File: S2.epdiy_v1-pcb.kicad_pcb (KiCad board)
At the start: 4 copper layers, 99.1 x 58.9 mm, 80 parts, among them J1 USB_C_Receptacle_USB2.0, J2 Jack-DC, SW1 RESET, SW2 BOOT, U1 MCP1700-1202E_SOT23, U11 TP4056, U2 ESP32-S2-WROVER, U3 TPS651851RSLR, U6 ED060XC5, U7 TPS2113APW

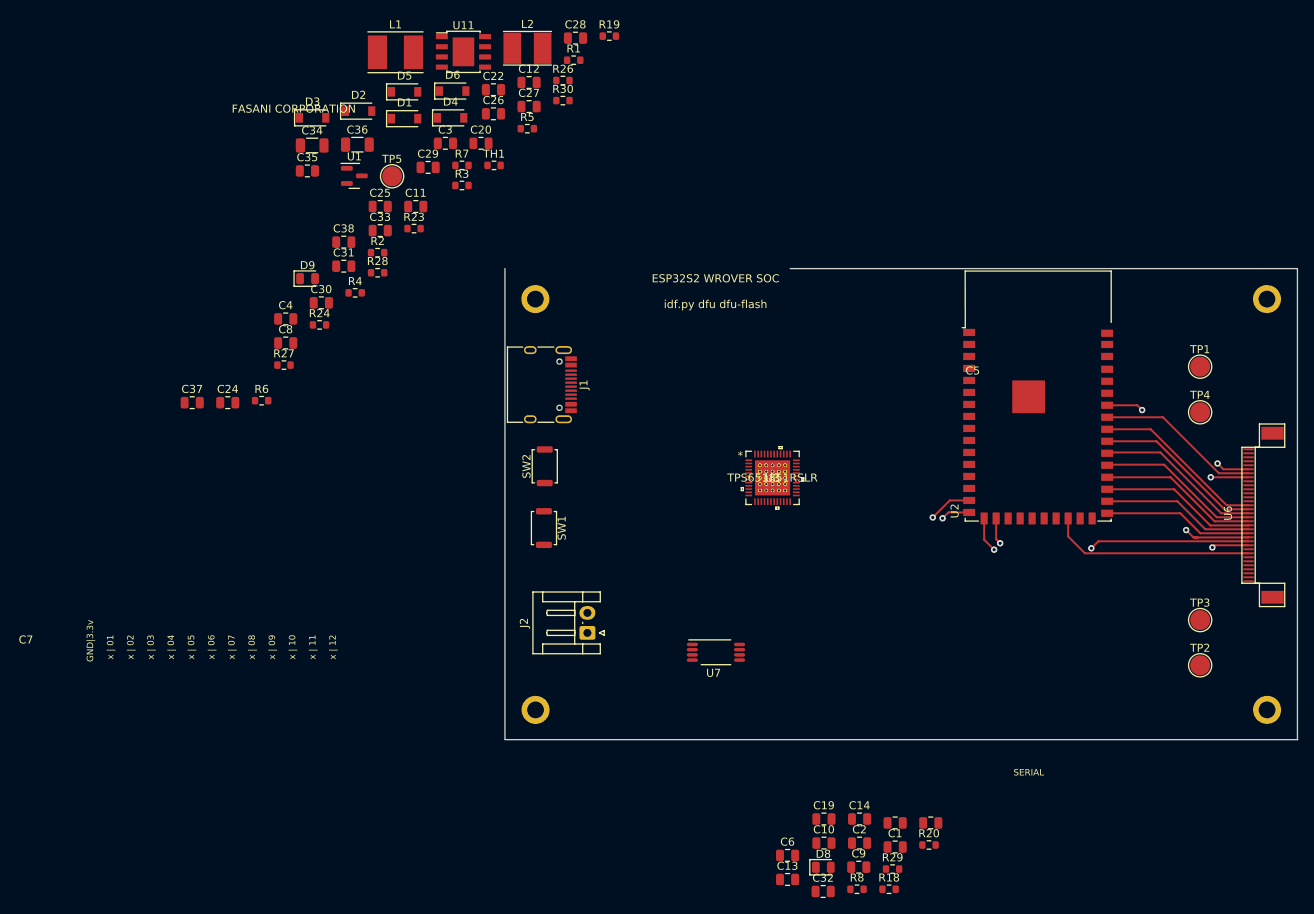
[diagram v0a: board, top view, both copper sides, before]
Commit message: Routing v1. Pending ERC pass
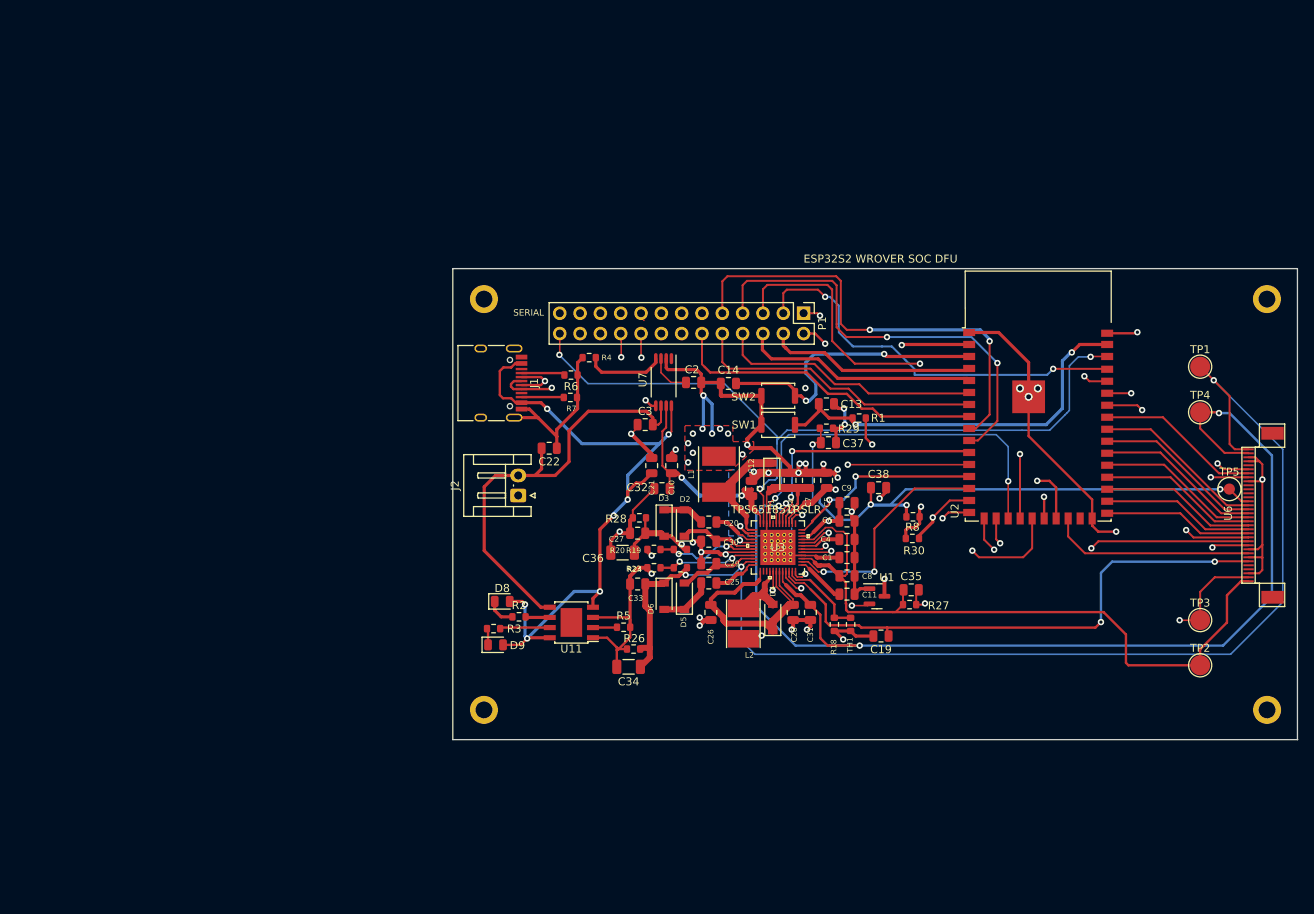
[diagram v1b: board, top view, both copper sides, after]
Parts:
- added C21: 0.1uF, Capacitor_SMD:C_0805_2012Metric, F.Cu at (114.9, 95.7)
- added P1: CONN_02X13, Connector_PinHeader_2.54mm:PinHeader_2x13_P2.54mm_Vertical, F.Cu at (133.8, 76.7)
- moved TP5 111.7 mm to (187.1, 98.7)
- moved C35 91.9 mm to (147.3, 111.3)
- moved U1 83.8 mm to (143.0, 112.1)
- moved R27 83.7 mm to (147.1, 113.1)
- moved C37 79.7 mm to (136.9, 92.9)
- moved L2 76.8 mm to (126.3, 115.5), turned to 90 degrees
- moved C28 76.8 mm to (132.5, 114.1), turned to 90 degrees
- moved C34 76.2 mm to (112.0, 120.9), turned to 180 degrees
- moved C8 76.0 mm to (139.3, 109.5), turned to 180 degrees
- moved C4 75.4 mm to (139.3, 105.0), turned to 180 degrees
- moved D4 74.3 mm to (130.0, 114.7), turned to 90 degrees
- moved C38 73.6 mm to (143.2, 98.5)
- moved TH1 72.7 mm to (139.7, 115.6), turned to -90 degrees
- moved C31 72.6 mm to (134.7, 114.1), turned to 90 degrees
- moved U11 72.6 mm to (104.8, 115.4), turned to 180 degrees
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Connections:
- C13 pad 1: GND -> Net-(C13-Pad1)
- C13 pad 2: Net-(C13-Pad2) -> GND
- R1 pad 1: /3.3v -> /+3.3V
- R1 pad 2: Net-(C13-Pad2) -> Net-(C13-Pad1)
- SW1 pad 1: Net-(C13-Pad2) -> Net-(C13-Pad1)
- U1 pad 2: /3.3v -> /+3.3V
- U2 pad 11: /IO08 -> /SCL
- U2 pad 12: /IO09 -> /SDA
- U2 pad 13: /IO10 -> /TPS_VCOM_CTRL
- U2 pad 14: /IO11 -> /TPS_nINT
- U2 pad 2: /3.3v -> /+3.3V
- U2 pad 20: /TPS_VCOM_CTRL -> /IO17
- U2 pad 39: /TPS_nINT -> /IO45
- U2 pad 41: Net-(C13-Pad2) -> Net-(C13-Pad1)
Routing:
- net GND: track 0.00 -> 262.9 mm, vias 0 -> 51
- net /15V: track 0.00 -> 157.4 mm, vias 0 -> 4
- net /+22V: track 0.00 -> 153.7 mm, vias 0 -> 3
- net /-20V: track 0.00 -> 106.2 mm, vias 0 -> 3
- net /TPS_PWR_GOOD: track 0.00 -> 95.8 mm, vias 0 -> 3
- net VBUS: track 0.00 -> 92.3 mm, vias 0 -> 7
- net /TX: track 0.00 -> 91.1 mm, vias 0 -> 1
- net SW_VIN: track 0.00 -> 90.5 mm, vias 0 -> 5
- net /-15V: track 0.00 -> 89.1 mm
- net Net-(J1-PadA6): track 0.00 -> 84.5 mm, vias 0 -> 3
- net Net-(J1-PadA7): track 0.00 -> 84.0 mm, vias 0 -> 2
- net /+3.3V: track 0.00 -> 78.3 mm, vias 0 -> 5
- net /RX: track 0.00 -> 76.2 mm, vias 0 -> 1
- net /EP_VCOM: track 0.00 -> 74.5 mm, vias 0 -> 4
- net EPD_VDD: track 0.00 -> 69.9 mm, vias 0 -> 2
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- added copper zone on B.Cu, net /VNEG_IN
- added copper zone on F.Cu, net GND
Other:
- board size 99.1 x 58.9 mm -> 105.6 x 58.9 mm
- board text added: "ESP32S2 WROVER SOC DFU"
- board text removed: "ESP32S2 WROVER SOC idf.py dfu dfu-flash"
- board text removed: "FASANI CORPORATION"
- board text removed: "GND|3.3v"
- board text removed: "x | 01"
- board text removed: "x | 02"
- board text removed: "x | 03"
- board text removed: "x | 04"
- board text removed: "x | 05"
- board text removed: "x | 06"
- board text removed: "x | 07"
- board text removed: "x | 08"
- board text removed: "x | 09"
- board text removed: "x | 10"
- board text removed: "x | 11"
- board text removed: "x | 12"

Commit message: V1 141 DRC pending
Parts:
- U2: footprint RF_Module:ESP32-S2-WROVER -> footprint:ESP32-S2-WROVER
- moved R4 2.36 mm to (108.0, 84.4)
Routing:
- net Net-(R4-Pad1): track 9.90 -> 7.72 mm
- net /SCL: track 58.6 -> 60.6 mm
- net /TPS_PWR_GOOD: track 95.8 -> 97.1 mm
- net GND: track 262.9 -> 262.0 mm
- net /SDA: track 63.9 -> 64.7 mm
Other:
- board text added: "17"
- board text added: "18"
- board text added: "20"
- board text added: "26"
- board text added: "3.3v"
- board text added: "DAC"
- board text added: "ESP32S2 WROVER SOC"
- board text added: "FASANI CORPORATION"
- board text added: "GND"
- board text added: "IO01"
- board text added: "IO02"
- board text added: "IO03"
- board text added: "IO04"
- board text added: "IO05"
- board text added: "IO06"
- board text added: "IO07"
- board text added: "IO45"
- board text added: "RX"
- board text added: "SDA>"
- board text added: "SDL>"
- board text added: "TX"
- board text added: "x"
- board text removed: "ESP32S2 WROVER SOC DFU"

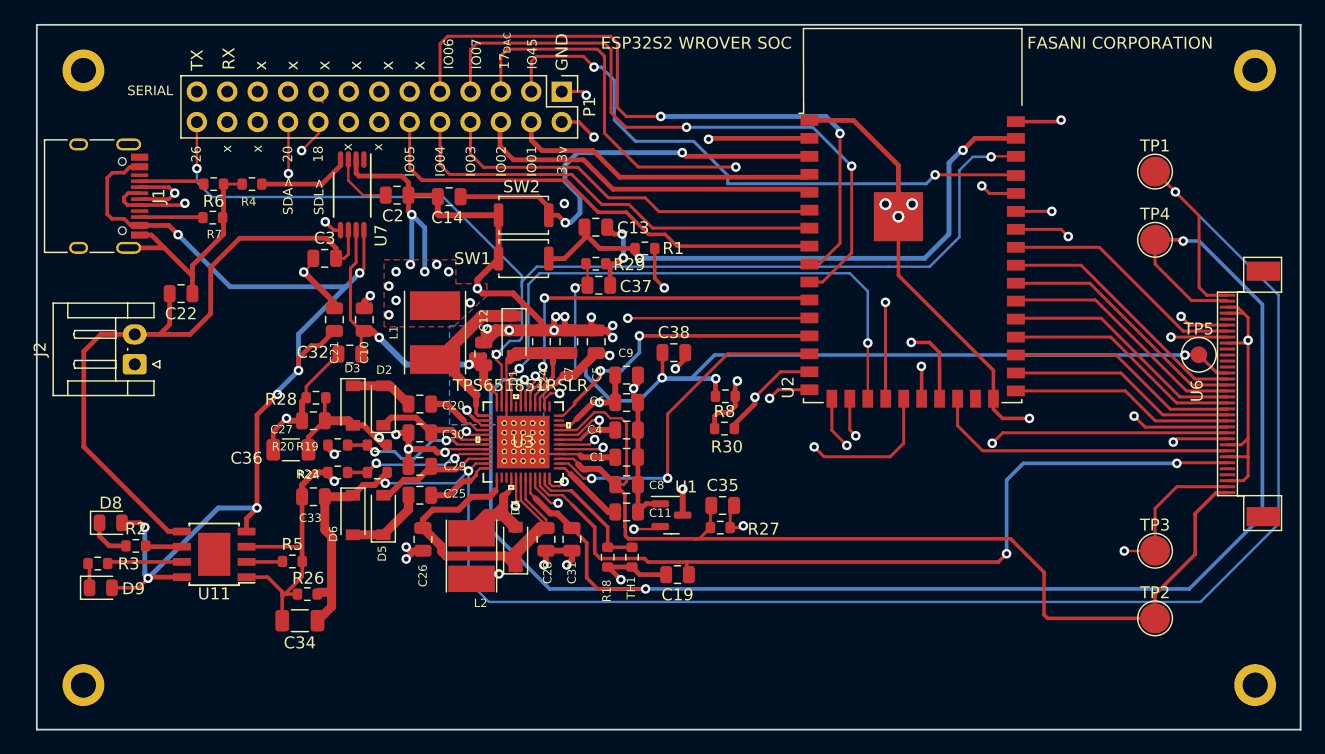
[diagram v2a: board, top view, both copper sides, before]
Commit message: Update C recommended to be close to EPD
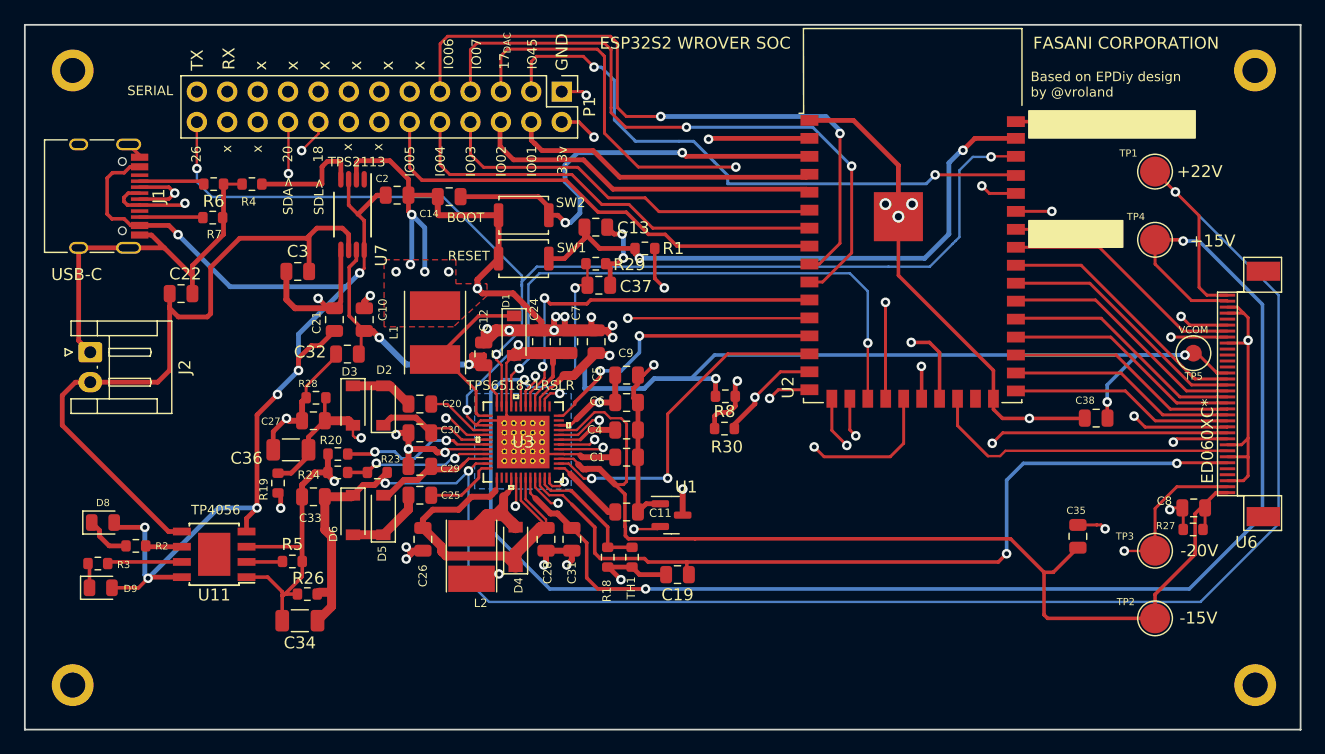
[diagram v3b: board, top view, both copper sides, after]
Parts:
- moved C8 47.4 mm to (186.7, 111.5), turned to 0 degrees
- moved R27 39.5 mm to (186.6, 113.3), turned to 180 degrees
- moved C38 35.7 mm to (178.5, 104.0), turned to 180 degrees
- moved C35 29.8 mm to (177.0, 113.8), turned to 90 degrees
- moved R19 8.88 mm to (110.2, 109.4), turned to -90 degrees
- moved J2 3.84 mm to (94.5, 98.5), turned to -90 degrees
- moved C3 2.50 mm to (111.8, 91.7)
- moved U7 1.65 mm to (116.4, 87.0)
- moved MK1 0.89 mm to (93.0, 126.3)
- moved MK2 0.89 mm to (93.0, 74.9)
- moved R20 0.75 mm to (115.2, 107.0)
- moved D8 0.65 mm to (95.5, 112.7)
- moved TP5 0.46 mm to (186.6, 98.5)
- moved C32 0.20 mm to (116.0, 98.6)
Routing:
- net GND: track 262.0 -> 290.6 mm, vias 51 -> 44
- net Net-(R19-Pad2): track 12.9 -> 23.9 mm, vias 2 -> 3
- net /EP_VCOM: track 74.5 -> 82.6 mm
- net /-20V: track 106.2 -> 109.5 mm
- net BAT+: track 54.5 -> 57.5 mm
- net SW_VIN: track 90.5 -> 87.7 mm
- net /VNEG_IN: track 35.8 -> 38.3 mm, vias 1 -> 2
- net /-15V: track 89.1 -> 91.2 mm
- net VBUS: track 92.3 -> 94.4 mm
- net Net-(R4-Pad1): track 7.72 -> 9.65 mm
- net Net-(J1-PadA6): vias 3 -> 2
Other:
- board size 105.6 x 58.9 mm -> 106.6 x 58.9 mm
- board text added: "+15V"
- board text added: "+22V"
- board text added: "-15V"
- board text added: "-20V"
- board text added: "BOOT"
- board text added: "Based on EPDiy design by @vroland"
- board text added: "ED060XC*"
- board text added: "RESET"
- board text added: "TP4056"
- board text added: "TPS2113"
- board text added: "USB-C"
- board text added: "VCOM"
